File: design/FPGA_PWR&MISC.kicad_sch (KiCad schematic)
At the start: 123 parts

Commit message: new power converter added
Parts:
- C1, C222, C225, C280, C281, C282, C283, C384, C385: renamed from C?; value (none) -> CC0603_22UF_6.3V_20%_X5R; footprint (none) -> CAPC1709X100N
- C2, C239, C265, C266: value (none) -> CC1210_100UF_6.3V_20%_X5R; footprint (none) -> CAPC3225X270N
- C216, C223, C226, C227, C228, C229, C231, C244, C245, C246, C247, C248, C249, C250, C251, C256, C257, C258, C259, C260, C261, C262, C263, C264, C267, C269, C271, C273, C275, C277, C279, C3, C332, C333, C334, C335, C336, C337, C338, C339, C380, C381, C387, C388, C389, C390, C391, C392, C4: value (none) -> CC0201_470NF_4V_20%_X5R; footprint (none) -> CAPC0603X33N
- C217, C218, C219, C220, C221, C224, C230, C232, C234, C236, C238, C418, C419, C420, C421: renamed from C?; value (none) -> CC0201_100NF_6.3V_10%_X5R; footprint (none) -> CAPC0603X33N
- C233, C235, C237, C240, C241, C242, C243, C252, C253, C254, C255, C268, C270, C272, C274, C276, C278, C284, C285, C286, C287, C386: value (none) -> CC0805_4.7UF_10V_10%_X5R; footprint (none) -> CAPC2012X135N
- D1, D9: renamed from D?; value (none) -> BAT165; footprint (none) -> ICs And Semiconductors SMD:SOD2512X110N
- L27, L28: renamed from L?; value (none) -> IND0603_MURATA_BLM18SG121TN1D; footprint (none) -> INDC1608X65N
- LD3: value (none) -> LED_KINGBRIGHT_KPH-1608CGCK; footprint (none) -> ICs And Semiconductors SMD:LED_KINGBRIGHT_KPH-1608CGCK
- Q19, Q21: value (none) -> BSS138L; footprint (none) -> ICs And Semiconductors SMD:SOT95P240X110-3N
- R159, R286, R287, R288: renamed from R?; value (none) -> R0402_0R_JUMPER; footprint (none) -> RESC1005X40N
- R160: renamed from R?; value (none) -> R0402_2K2_1%_0.0625W_100PPM; footprint (none) -> RESC1005X40N
- R161: renamed from R?; value (none) -> R0402_100R_1%_0.1W_100PPM; footprint (none) -> RESC1005X40N
- R162: value (none) -> R0402_300R_1%_0.0625W_100PPM; footprint (none) -> RESC1005X40N
- R163, R283, R284, R285: value (none) -> R0402_1K_1%_0.0625W_100PPM; footprint (none) -> RESC1005X40N
- R282: value (none) -> R0402_4K7_1%_0.0625W_100PPM; footprint (none) -> Resistors SMD:RESC1005X40N
- SW5: renamed from SW?; value (none) -> KSS241GLFS; footprint (none) -> Marble:KSS241GLFS
- U1: renamed from U?; value (none) -> XC7K160T-2FFG676C; footprint (none) -> ICs And Semiconductors SMD_BGA:BGA676C100P26X26_2700X2700X260
- U60: renamed from U?; value (none) -> TPS3703A7330DSER; footprint (none) -> ICs And Semiconductors SMD:SON50P150X150X80-6N

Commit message: connected signals to the J9 connector
connected signals to the J9 connector
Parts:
- C1, C2, C216, C217, C218, C219, C220, C221, C222, C223, C224, C225, C226, C227, C228, C229, C230, C231, C232, C233, C234, C235, C236, C237, C238, C239, C240, C241, C242, C243, C244, C245, C246, C247, C248, C249, C250, C251, C252, C253, C254, C255, C256, C257, C258, C259, C260, C261, C262, C263, C264, C265, C266, C267, C268, C269, C270, C271, C272, C273, C274, C275, C276, C277, C278, C279, C280, C281, C282, C283, C284, C285, C286, C287, C3, C332, C333, C334, C335, C336, C337, C338, C339, C380, C381, C384, C385, C386, C387, C388, C389, C390, C391, C392, C4, C418, C419, C420, C421, L27, L28, R159, R160, R161, R162, R163, R282, R283, R284, R285, R286, R287, R288: Author CERN DEM JLC -> (none)
- D1, D9, Q19, Q21: Author CERN DEM JLC -> (none); Bonding No -> (none)
- LD3: Author CERN DEM JLC -> (none); Bonding No -> (none); Color Green -> (none)

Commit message: Attempt to add and improve BOM. Added new part numbers for some of the passives
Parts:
- C2, C239, C265, C266, R159, R286, R287, R288: MANUFACTURER (none) -> GENERIC
- R161: MANUFACTURER (none) -> GENERIC; Manufacturer Part Number R0402_100R_1%_0.1W_100PPM_50V -> R0402_100R_1%_0.1W_100PPM
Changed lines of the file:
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@@
     )
     (property "config" "dnf" (id 41) (at 326.39 121.92 0))
+    (property "MANUFACTURER" "GENERIC" (id 42) (at 316.23 123.19 0)
+      (effects (font (size 1.27 1.27)) hide)
+    )
     (pin "1")
     (pin "2")
@@
     )
     (property "config" "dnf" (id 41) (at 326.39 124.46 0))
+    (property "MANUFACTURER" "GENERIC" (id 42) (at 316.23 125.73 0)
+      (effects (font (size 1.27 1.27)) hide)
+    )
     (pin "1")
     (pin "2")
@@
     )
     (property "config" "dnf" (id 41) (at 326.39 127 0))
+    (property "MANUFACTURER" "GENERIC" (id 42) (at 316.23 128.27 0)
+      (effects (font (size 1.27 1.27)) hide)
+    )
     (pin "1")
     (pin "2")
@@
       (effects (font (size 1.524 1.524)) (justify left) hide)
     )
+    (property "MANUFACTURER" "GENERIC" (id 40) (at 132.08 240.03 0)
+      (effects (font (size 1.27 1.27)) hide)
+    )
     (pin "1")
     (pin "2")
@@
       (effects (font (size 1.524 1.524)) (justify left) hide)
     )
+    (property "MANUFACTURER" "GENERIC" (id 40) (at 17.78 264.16 0)
+      (effects (font (size 1.27 1.27)) hide)
+    )
     (pin "1")
     (pin "2")
@@
       (effects (font (size 1.524 1.524)) (justify left) hide)
     )
+    (property "MANUFACTURER" "GENERIC" (id 40) (at 241.3 240.03 0)
+      (effects (font (size 1.27 1.27)) hide)
+    )
     (pin "1")
     (pin "2")
@@
       (effects (font (size 1.524 1.524)) (justify left) hide)
     )
+    (property "MANUFACTURER" "GENERIC" (id 40) (at 247.65 240.03 0)
+      (effects (font (size 1.27 1.27)) hide)
+    )
     (pin "1")
     (pin "2")
@@
       (effects (font (size 1.524 1.524)) (justify left) hide)
     )
+    (property "MANUFACTURER" "GENERIC" (id 41) (at 274.32 153.67 0)
+      (effects (font (size 1.27 1.27)) hide)
+    )
     (pin "1")
     (pin "2")
@@
       (effects (font (size 1.524 1.524)) (justify left) hide)
     )
-    (property "Manufacturer Part Number" "R0402_100R_1%_0.1W_100PPM_50V" (id 23) (at 285.75 117.856 0)
+    (property "Manufacturer Part Number" "R0402_100R_1%_0.1W_100PPM" (id 23) (at 285.75 117.856 0)
       (effects (font (size 1.524 1.524)) (justify left) hide)
     )
@@
       (effects (font (size 1.524 1.524)) (justify left) hide)
     )
+    (property "MANUFACTURER" "GENERIC" (id 41) (at 285.75 62.23 0)
+      (effects (font (size 1.27 1.27)) hide)
+    )
     (pin "1")

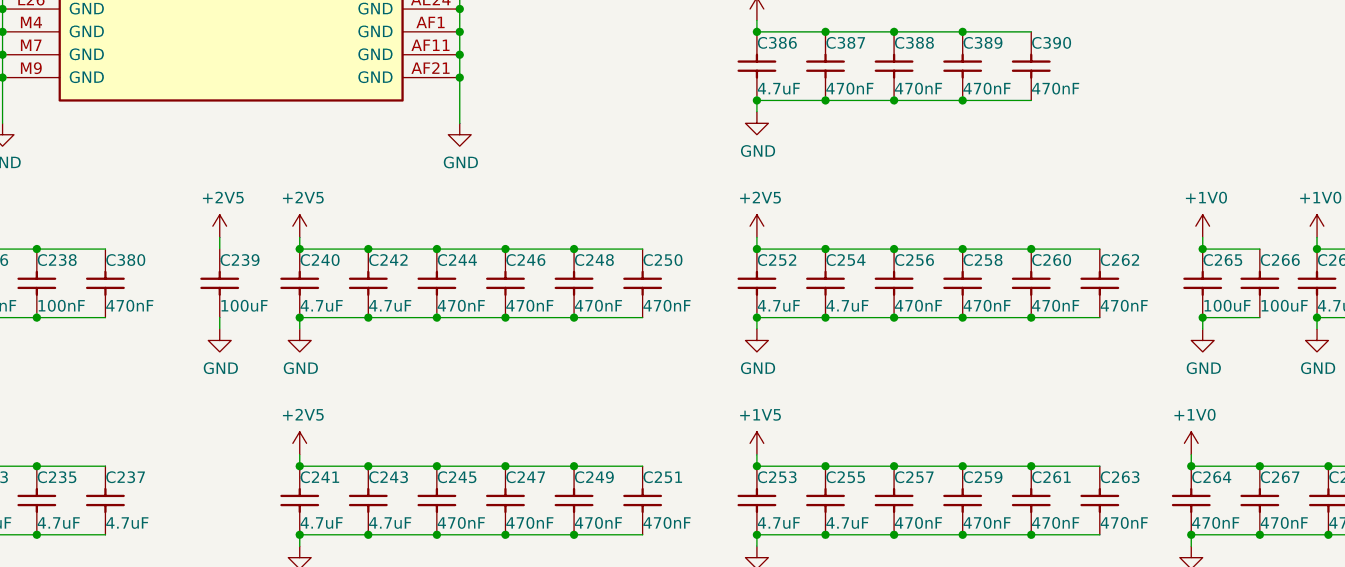
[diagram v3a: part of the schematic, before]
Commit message: Fixed part numbers for C127 and D10
Fixed part numbers for C127 and D10
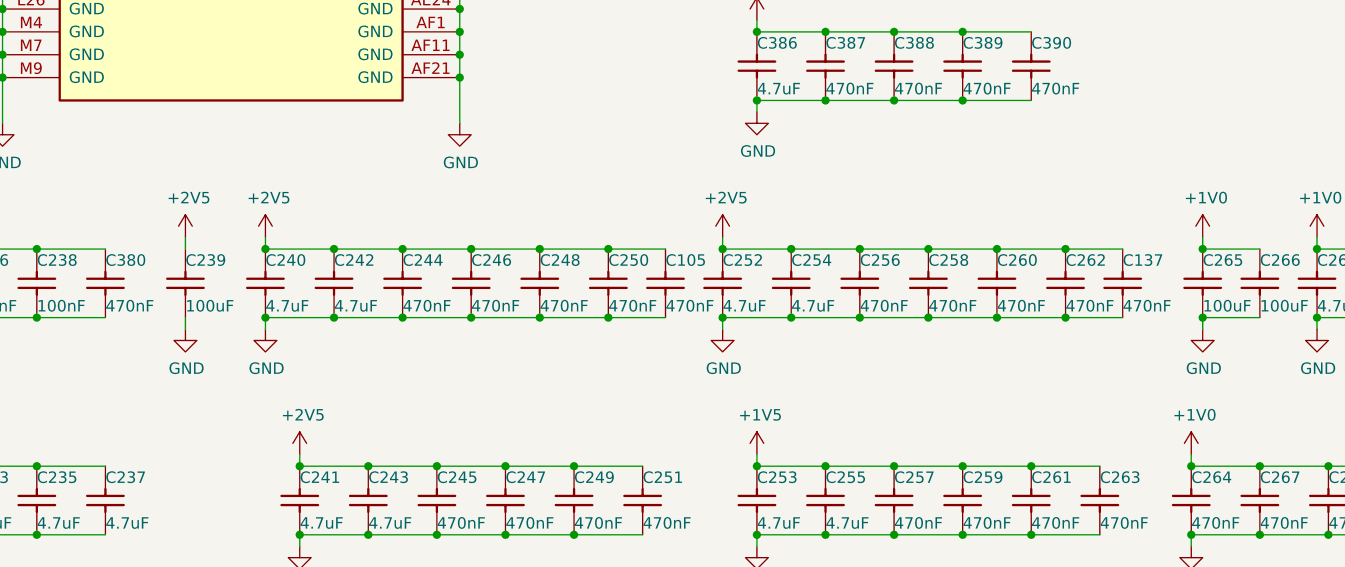
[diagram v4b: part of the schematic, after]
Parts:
- added C105, C137: CC0201_470NF_4V_20%_X5R, CAPC0603X33N, symbol Capacitors_SMD:CC0201_470NF_4V_20%_X5R
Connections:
- net +2V5: now also C105.1, C137.1
- net GND: now also C105.2, C137.2
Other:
- moved on the sheet: C239, C240, C242, C244, C246, C248, C250, C252, C254, C256, C258, C260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

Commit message: Restore some consistency in schematic metadata
Still 13 problematic footprint names in LTM4673.kicad_sch:

BAD Dup: "Footprint" "CAPC1608X87N" "Capacitors SMD:CAPC1005X55N" in LTM4673-altium-import:0_Capacitor - non polarized
BAD Dup: "Footprint" "CAPC2012X135N" "CAPC1608X87N" in LTM4673-altium-import:1_Capacitor - non polarized
BAD Dup: "Footprint" "CAPC1608X87N" "Capacitors SMD:CAPC1005X55N" in LTM4673-altium-import:1_Capacitor - non polarized
BAD Dup: "Footprint" "CAPC3216X180N" "CAPC3225X270N" in LTM4673-altium-import:1_Capacitor - non polarized
BAD Dup: "Footprint" "CAPC1608X87N" "Capacitors SMD:CAPC1005X55N" in LTM4673-altium-import:0_Capacitor - non polarized
BAD Dup: "Footprint" "CAPC1608X87N" "Capacitors SMD:CAPC1005X55N" in LTM4673-altium-import:0_Capacitor - non polarized
BAD Dup: "Footprint" "CAPC3216X180N" "CAPC3225X270N" in LTM4673-altium-import:1_Capacitor - non polarized
BAD Dup: "Footprint" "CAPC2012X135N" "CAPC1608X87N" in LTM4673-altium-import:1_Capacitor - non polarized
BAD Dup: "Footprint" "CAPC3216X180N" "CAPC3225X270N" in LTM4673-altium-import:1_Capacitor - non polarized
BAD Dup: "Footprint" "CAPC1608X87N" "Capacitors SMD:CAPC1005X55N" in LTM4673-altium-import:0_Capacitor - non polarized
BAD Dup: "Footprint" "CAPC1608X87N" "Capacitors SMD:CAPC1005X55N" in LTM4673-altium-import:1_Capacitor - non polarized
BAD Dup: "Footprint" "CAPC3216X180N" "CAPC3225X270N" in LTM4673-altium-import:1_Capacitor - non polarized
BAD Dup: "Footprint" "CAPMP7343X310N" "Capacitor_Tantalum_SMD:CP_EIA-7343-30_AVX-N" in LTM4673-altium-import:3_Capacitor - polarized

But the Symbol Field editor in eeschema should be more useful now.
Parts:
- C2, C239, C265, C266, R159, R161, R286, R287, R288: MANUFACTURER GENERIC -> (none)
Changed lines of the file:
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@@
     )
     (property "config" "dnf" (id 41) (at 326.39 121.92 0))
-    (property "MANUFACTURER" "GENERIC" (id 42) (at 316.23 123.19 0)
-      (effects (font (size 1.27 1.27)) hide)
-    )
     (pin "1")
     (pin "2")
@@
     )
     (property "config" "dnf" (id 41) (at 326.39 124.46 0))
-    (property "MANUFACTURER" "GENERIC" (id 42) (at 316.23 125.73 0)
-      (effects (font (size 1.27 1.27)) hide)
-    )
     (pin "1")
     (pin "2")
@@
     )
     (property "config" "dnf" (id 41) (at 326.39 127 0))
-    (property "MANUFACTURER" "GENERIC" (id 42) (at 316.23 128.27 0)
-      (effects (font (size 1.27 1.27)) hide)
-    )
     (pin "1")
     (pin "2")
@@
       (effects (font (size 1.524 1.524)) (justify left) hide)
     )
-    (property "MANUFACTURER" "GENERIC" (id 40) (at 128.27 240.03 0)
-      (effects (font (size 1.27 1.27)) hide)
-    )
     (pin "1")
     (pin "2")
@@
       (effects (font (size 1.524 1.524)) (justify left) hide)
     )
-    (property "MANUFACTURER" "GENERIC" (id 40) (at 17.78 264.16 0)
-      (effects (font (size 1.27 1.27)) hide)
-    )
     (pin "1")
     (pin "2")
@@
       (effects (font (size 1.524 1.524)) (justify left) hide)
     )
-    (property "MANUFACTURER" "GENERIC" (id 40) (at 241.3 240.03 0)
-      (effects (font (size 1.27 1.27)) hide)
-    )
     (pin "1")
     (pin "2")
@@
       (effects (font (size 1.524 1.524)) (justify left) hide)
     )
-    (property "MANUFACTURER" "GENERIC" (id 40) (at 247.65 240.03 0)
-      (effects (font (size 1.27 1.27)) hide)
-    )
     (pin "1")
     (pin "2")
@@
       (effects (font (size 1.524 1.524)) (justify left) hide)
     )
-    (property "MANUFACTURER" "GENERIC" (id 41) (at 274.32 153.67 0)
-      (effects (font (size 1.27 1.27)) hide)
-    )
     (pin "1")
     (pin "2")
@@
       (effects (font (size 1.524 1.524)) (justify left) hide)
     )
-    (property "MANUFACTURER" "GENERIC" (id 41) (at 285.75 62.23 0)
-      (effects (font (size 1.27 1.27)) hide)
-    )
     (pin "1")

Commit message: Parts substitutions and a reproducibility tweak
INFINEON BAT165E6327HTSA1 becomes NEXPERIA BAT165AX (it was actually like this before)
Murata GRM155R61A225ME95D becomes Taiyo Yuden JMK105BJ225KV-F
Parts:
- D1, D9: Manufacturer INFINEON -> NEXPERIA; Manufacturer Part Number BAT165E6327HTSA1 -> BAT165AX
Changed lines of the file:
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@@
       (effects (font (size 1.524 1.524)) (justify left) hide)
     )
-    (property "Manufacturer" "INFINEON" (id 16) (at 241.808 189.23 0)
+    (property "Manufacturer" "NEXPERIA" (id 16) (at 241.808 189.23 0)
       (effects (font (size 1.524 1.524)) (justify left) hide)
     )
-    (property "Manufacturer Part Number" "BAT165E6327HTSA1" (id 17) (at 239.522 189.23 0)
+    (property "Manufacturer Part Number" "BAT165AX" (id 17) (at 239.522 189.23 0)
       (effects (font (size 1.524 1.524)) (justify left) hide)
     )
@@
       (effects (font (size 1.524 1.524)) (justify left) hide)
     )
-    (property "Manufacturer" "INFINEON" (id 16) (at 260.858 189.23 0)
+    (property "Manufacturer" "NEXPERIA" (id 16) (at 260.858 189.23 0)
       (effects (font (size 1.524 1.524)) (justify left) hide)
     )
-    (property "Manufacturer Part Number" "BAT165E6327HTSA1" (id 17) (at 258.572 189.23 0)
+    (property "Manufacturer Part Number" "BAT165AX" (id 17) (at 258.572 189.23 0)
       (effects (font (size 1.524 1.524)) (justify left) hide)
     )
